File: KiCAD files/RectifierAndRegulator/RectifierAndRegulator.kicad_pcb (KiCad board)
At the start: 2 copper layers, 73.7 x 25.4 mm, 11 parts, among them J1 Input, J2 Output, U1 L7805

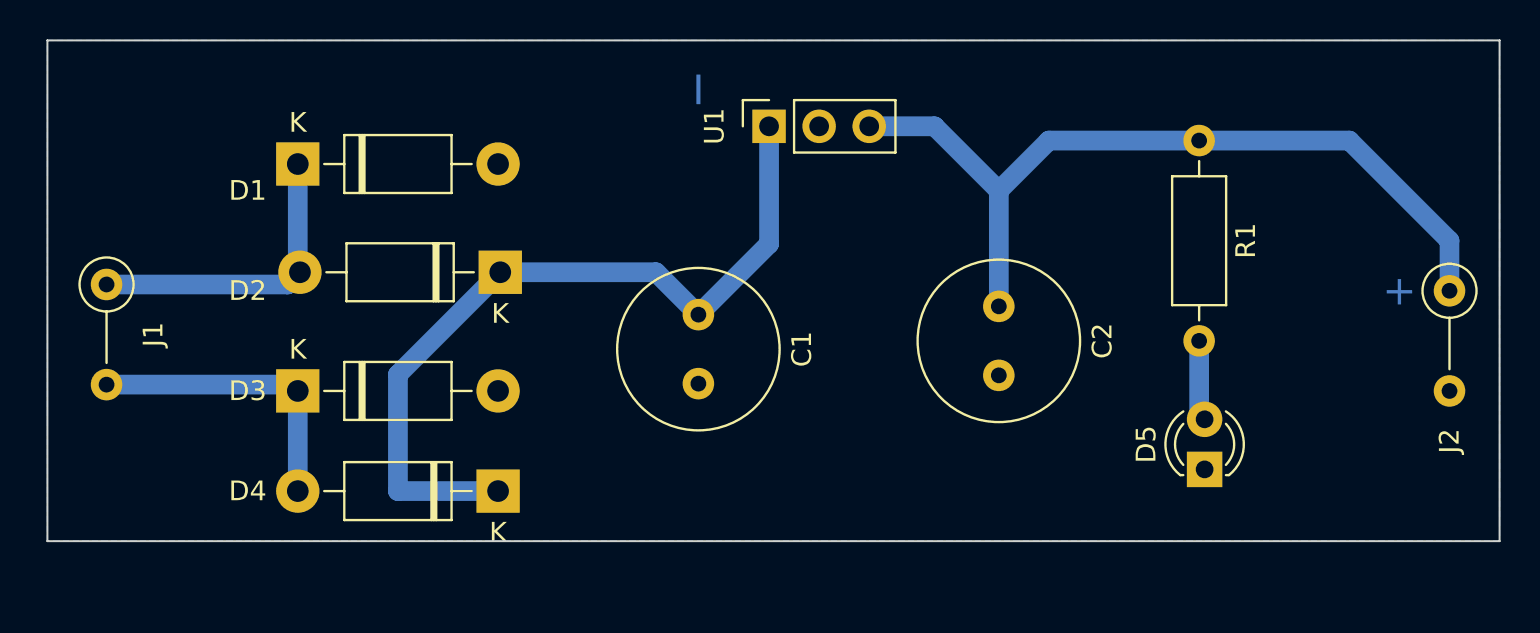
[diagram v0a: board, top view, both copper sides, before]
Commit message: Edited Rectifier schematics and PCB
edited the trackwidth from 1mm to 1.5mm
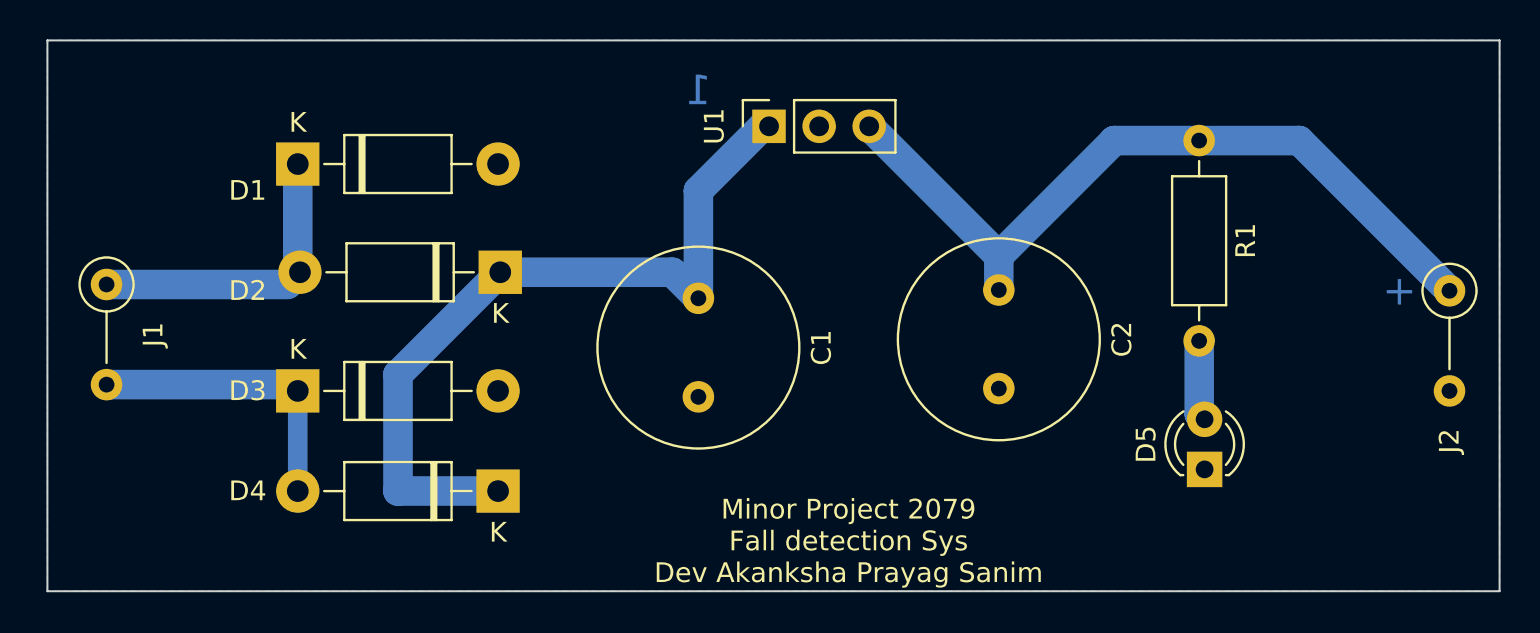
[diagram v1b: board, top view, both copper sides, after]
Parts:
- C1, C2: footprint Capacitor_THT:C_Radial_D8.0mm_H7.0mm_P3.50mm -> Capacitor_THT:C_Radial_D10.0mm_H20.0mm_P5.00mm
- R1: value 470/220 -> 470
- moved C1 0.83 mm to (101.6, 122.3)
- moved C2 0.83 mm to (116.8, 121.9)
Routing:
- net Net-(C2-Pad1): track 42.4 -> 39.5 mm
- net unconnected-(C1-Pad1): track 40.3 -> 39.3 mm
- net GND: track 0.89 -> 0.30 mm
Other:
- board size 73.7 x 25.4 mm -> 73.7 x 27.9 mm
- board text added: "1"
- board text added: "Minor Project 2079 Fall detection Sys Dev Akanksha Prayag Sanim"
- board text removed: "I"

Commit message: Edited PCB
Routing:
- net unconnected-(C1-Pad1): track 39.3 -> 21.1 mm
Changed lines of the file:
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@@
     (effects (font (size 1 1) (thickness 0.15)))
   )
-  (segment (start 81.28 115.49) (end 81.28 120.87) (width 1.5) (layer "B.Cu") (net 1))
+  (segment (start 81.39 120.98) (end 81.39 115.6) (width 1) (layer "B.Cu") (net 1))
+  (segment (start 81.39 115.6) (end 81.28 115.49) (width 1) (layer "B.Cu") (net 1))
   (segment (start 71.58 121.6) (end 80.77 121.6) (width 1.5) (layer "B.Cu") (net 1))
   (segment (start 80.77 121.6) (end 81.39 120.98) (width 1) (layer "B.Cu") (net 1))
   (segment (start 81.28 120.87) (end 81.39 120.98) (width 1.5) (layer "B.Cu") (net 1))
   (segment (start 91.65 126.79) (end 91.44 127) (width 0.25) (layer "B.Cu") (net 2))
-  (segment (start 101.6 116.84) (end 101.6 122.3) (width 1.5) (layer "B.Cu") (net 3))
   (segment (start 105.185 113.5775) (end 104.8625 113.5775) (width 1.5) (layer "B.Cu") (net 3))
-  (segment (start 86.36 126.17) (end 86.36 132.08) (width 1.5) (layer "B.Cu") (net 3))
-  (segment (start 104.8625 113.5775) (end 101.6 116.84) (width 1.5) (layer "B.Cu") (net 3))
-  (segment (start 91.55 120.98) (end 86.36 126.17) (width 1.5) (layer "B.Cu") (net 3))
-  (segment (start 91.55 120.98) (end 100.28 120.98) (width 1.5) (layer "B.Cu") (net 3))
-  (segment (start 86.36 132.08) (end 91.44 132.08) (width 1.5) (layer "B.Cu") (net 3))
-  (segment (start 100.28 120.98) (end 101.6 122.3) (width 1.5) (layer "B.Cu") (net 3))
-  (segment (start 122.6925 114.3) (end 116.84 120.1525) (width 1.5) (layer "B.Cu") (net 4))
-  (segment (start 116.84 121.88) (end 116.84 120.1525) (width 1.5) (layer "B.Cu") (net 4))
-  (segment (start 139.7 121.92) (end 132.08 114.3) (width 1.5) (layer "B.Cu") (net 4))
-  (segment (start 132.08 114.3) (end 127 114.3) (width 1.5) (layer "B.Cu") (net 4))
-  (segment (start 127 114.3) (end 122.6925 114.3) (width 1.5) (layer "B.Cu") (net 4))
-  (segment (start 116.84 120.1525) (end 110.265 113.5775) (width 1.5) (layer "B.Cu") (net 4))
-  (segment (start 127 128.16169) (end 127.277858 128.439548) (width 1.5) (layer "B.Cu") (net 5))
-  (segment (start 127 124.46) (end 127 128.16169) (width 1.5) (layer "B.Cu") (net 5))
+  (segment (start 91.55 120.98) (end 100.28 120.98) (width 1) (layer "B.Cu") (net 3))
+  (segment (start 100.28 120.98) (end 101.6 122.3) (width 1) (layer "B.Cu") (net 3))
+  (segment (start 101.6 122.3) (end 101.6 117.1625) (width 1) (layer "B.Cu") (net 3))
+  (segment (start 101.6 117.1625) (end 105.185 113.5775) (width 1) (layer "B.Cu") (net 3))
+  (segment (start 116.84 120.1525) (end 116.84 121.88) (width 1) (layer "B.Cu") (net 4))
+  (segment (start 122.6925 114.3) (end 116.84 120.1525) (width 1) (layer "B.Cu") (net 4))
+  (segment (start 139.7 121.92) (end 132.08 114.3) (width 1) (layer "B.Cu") (net 4))
+  (segment (start 132.08 114.3) (end 127 114.3) (width 1) (layer "B.Cu") (net 4))
+  (segment (start 127 114.3) (end 122.6925 114.3) (width 1) (layer "B.Cu") (net 4))
+  (segment (start 110.265 113.5775) (end 116.84 120.1525) (width 1) (layer "B.Cu") (net 4))
+  (segment (start 127 128.16169) (end 127.277858 128.439548) (width 1) (layer "B.Cu") (net 5))
+  (segment (start 127 124.46) (end 127 128.16169) (width 1) (layer "B.Cu") (net 5))
   (segment (start 80.96 126.68) (end 81.28 127) (width 1) (layer "B.Cu") (net 6))
   (segment (start 71.58 126.68) (end 80.96 126.68) (width 1.5) (layer "B.Cu") (net 6))
-  (segment (start 81.28 132.08) (end 81.28 127) (width 1) (layer "B.Cu") (net 6))
+  (segment (start 81.28 127) (end 81.28 132.08) (width 1) (layer "B.Cu") (net 6))
   (zone (net 2) (net_name "GND") (layer "B.Cu") (hatch edge 0.508)
     (connect_pads (clearance 0.508))

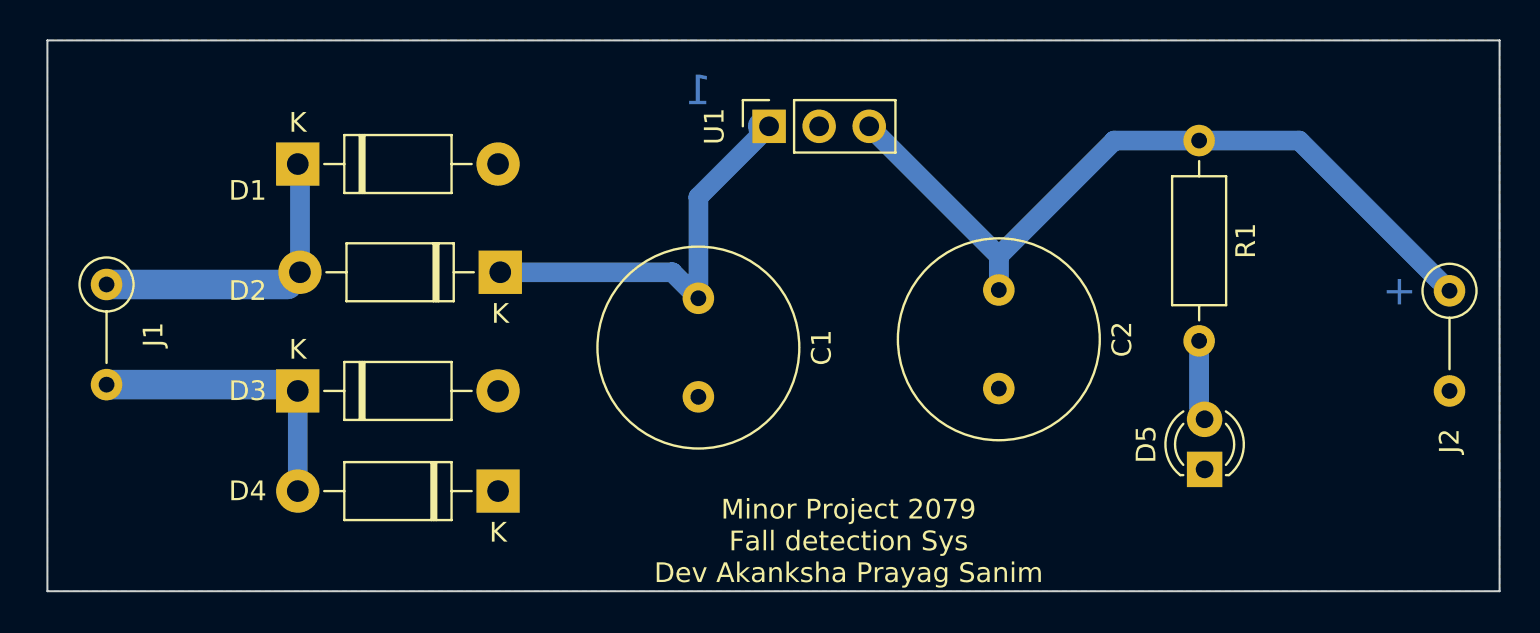
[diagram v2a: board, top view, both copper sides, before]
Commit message: Rectiier ckt bug fixed
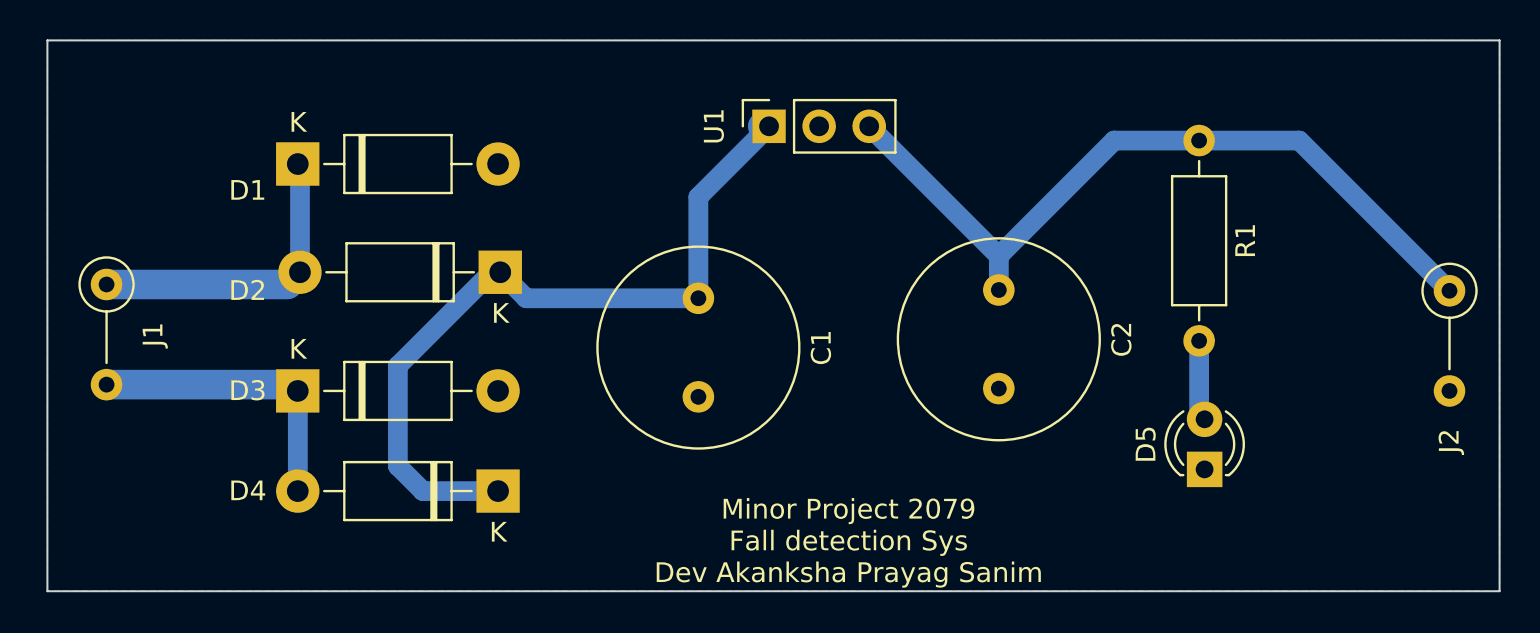
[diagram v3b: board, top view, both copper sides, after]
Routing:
- net unconnected-(C1-Pad1): track 21.1 -> 39.0 mm
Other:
- board text removed: "+"
- board text removed: "1"
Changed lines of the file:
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@@
   )
   (gr_rect (start 68.58 109.22) (end 142.24 137.16) (layer "Edge.Cuts") (width 0.1) (fill none))
-  (gr_text "1\n" (at 101.6 111.76) (layer "B.Cu")
-    (effects (font (size 1.5 1.5) (thickness 0.3)) (justify mirror))
-  )
-  (gr_text "+" (at 137.16 121.92) (layer "B.Cu")
-    (effects (font (size 1.5 1.5) (thickness 0.3)) (justify mirror))
-  )
   (gr_text "Minor Project 2079\nFall detection Sys\nDev Akanksha Prayag Sanim" (at 109.22 134.62) (layer "F.SilkS")
     (effects (font (size 1 1) (thickness 0.15)))
@@
   (segment (start 81.28 120.87) (end 81.39 120.98) (width 1.5) (layer "B.Cu") (net 1))
   (segment (start 91.65 126.79) (end 91.44 127) (width 0.25) (layer "B.Cu") (net 2))
+  (segment (start 91.11 120.98) (end 86.36 125.73) (width 1) (layer "B.Cu") (net 3))
+  (segment (start 92.87 122.3) (end 91.55 120.98) (width 1) (layer "B.Cu") (net 3))
   (segment (start 105.185 113.5775) (end 104.8625 113.5775) (width 1.5) (layer "B.Cu") (net 3))
-  (segment (start 91.55 120.98) (end 100.28 120.98) (width 1) (layer "B.Cu") (net 3))
-  (segment (start 100.28 120.98) (end 101.6 122.3) (width 1) (layer "B.Cu") (net 3))
+  (segment (start 86.36 130.81) (end 87.63 132.08) (width 1) (layer "B.Cu") (net 3))
+  (segment (start 101.6 122.3) (end 92.87 122.3) (width 1) (layer "B.Cu") (net 3))
+  (segment (start 91.55 120.98) (end 91.11 120.98) (width 1) (layer "B.Cu") (net 3))
   (segment (start 101.6 122.3) (end 101.6 117.1625) (width 1) (layer "B.Cu") (net 3))
+  (segment (start 87.63 132.08) (end 91.44 132.08) (width 1) (layer "B.Cu") (net 3))
   (segment (start 101.6 117.1625) (end 105.185 113.5775) (width 1) (layer "B.Cu") (net 3))
+  (segment (start 86.36 125.73) (end 86.36 130.81) (width 1) (layer "B.Cu") (net 3))
   (segment (start 116.84 120.1525) (end 116.84 121.88) (width 1) (layer "B.Cu") (net 4))
   (segment (start 122.6925 114.3) (end 116.84 120.1525) (width 1) (layer "B.Cu") (net 4))

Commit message: Edited rectifier pcb
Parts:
- moved D1 6.59 mm to (81.3, 122.1)
- moved D2 4.14 mm to (91.4, 116.8)
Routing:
- net GND: track 0.30 -> 73.4 mm
- net unconnected-(C1-Pad1): track 39.0 -> 45.4 mm
- net Net-(D1-Pad1): track 15.8 -> 15.1 mm
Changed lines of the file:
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@@
   )
   (footprint "Diode_THT:D_DO-41_SOD81_P10.16mm_Horizontal" (layer "F.Cu")
-    (at 91.55 120.98 180)
+    (at 91.44 116.84 180)
     (descr "Diode, DO-41_SOD81 series, Axial, Horizontal, pin pitch=10.16mm, , length*diameter=5.2*2.7mm^2, , http://www.diodes.com/_files/packages/DO-41%20(Plastic).pdf")
     (tags "Diode DO-41_SOD81 series Axial Horizontal pin pitch 10.16mm  length 5.2mm diameter 2.7mm")
@@
   )
   (footprint "Diode_THT:D_DO-41_SOD81_P10.16mm_Horizontal" (layer "F.Cu")
-    (at 81.28 115.49)
+    (at 81.28 122.08)
     (descr "Diode, DO-41_SOD81 series, Axial, Horizontal, pin pitch=10.16mm, , length*diameter=5.2*2.7mm^2, , http://www.diodes.com/_files/packages/DO-41%20(Plastic).pdf")
     (tags "Diode DO-41_SOD81 series Axial Horizontal pin pitch 10.16mm  length 5.2mm diameter 2.7mm")
@@
     (effects (font (size 1 1) (thickness 0.15)))
   )
-  (segment (start 81.39 120.98) (end 81.39 115.6) (width 1) (layer "B.Cu") (net 1))
-  (segment (start 81.39 115.6) (end 81.28 115.49) (width 1) (layer "B.Cu") (net 1))
-  (segment (start 71.58 121.6) (end 80.77 121.6) (width 1.5) (layer "B.Cu") (net 1))
-  (segment (start 80.77 121.6) (end 81.39 120.98) (width 1) (layer "B.Cu") (net 1))
-  (segment (start 81.28 120.87) (end 81.39 120.98) (width 1.5) (layer "B.Cu") (net 1))
+  (segment (start 80.8 121.6) (end 81.28 122.08) (width 1.5) (layer "B.Cu") (net 1))
+  (segment (start 71.58 121.6) (end 80.8 121.6) (width 1.5) (layer "B.Cu") (net 1))
+  (segment (start 81.28 116.84) (end 81.28 122.08) (width 1) (layer "B.Cu") (net 1))
+  (segment (start 91.74 127.3) (end 91.44 127) (width 1) (layer "B.Cu") (net 2))
+  (segment (start 101.6 127.3) (end 91.74 127.3) (width 1) (layer "B.Cu") (net 2))
+  (segment (start 127.277858 130.979548) (end 135.720452 130.979548) (width 1) (layer "B.Cu") (net 2))
+  (segment (start 107.725 121.175) (end 101.6 127.3) (width 1) (layer "B.Cu") (net 2))
+  (segment (start 116.42 127.3) (end 116.84 126.88) (width 1) (layer "B.Cu") (net 2))
   (segment (start 91.65 126.79) (end 91.44 127) (width 0.25) (layer "B.Cu") (net 2))
-  (segment (start 91.11 120.98) (end 86.36 125.73) (width 1) (layer "B.Cu") (net 3))
-  (segment (start 92.87 122.3) (end 91.55 120.98) (width 1) (layer "B.Cu") (net 3))
+  (segment (start 135.720452 130.979548) (end 139.7 127) (width 1) (layer "B.Cu") (net 2))
+  (segment (start 101.6 127.3) (end 116.42 127.3) (width 1) (layer "B.Cu") (net 2))
+  (segment (start 120.939548 130.979548) (end 116.84 126.88) (width 1) (layer "B.Cu") (net 2))
+  (segment (start 91.44 122.08) (end 91.44 127) (width 1) (layer "B.Cu") (net 2))
+  (segment (start 127.277858 130.979548) (end 120.939548 130.979548) (width 1) (layer "B.Cu") (net 2))
+  (segment (start 107.725 113.5775) (end 107.725 121.175) (width 1) (layer "B.Cu") (net 2))
+  (segment (start 96.14 116.84) (end 101.6 122.3) (width 1) (layer "B.Cu") (net 3))
   (segment (start 105.185 113.5775) (end 104.8625 113.5775) (width 1.5) (layer "B.Cu") (net 3))
-  (segment (start 86.36 130.81) (end 87.63 132.08) (width 1) (layer "B.Cu") (net 3))
-  (segment (start 101.6 122.3) (end 92.87 122.3) (width 1) (layer "B.Cu") (net 3))
-  (segment (start 91.55 120.98) (end 91.11 120.98) (width 1) (layer "B.Cu") (net 3))
+  (segment (start 88.9 116.84) (end 91.44 116.84) (width 1) (layer "B.Cu") (net 3))
+  (segment (start 91.44 132.08) (end 88.9 132.08) (width 1) (layer "B.Cu") (net 3))
+  (segment (start 86.36 129.54) (end 86.36 119.38) (width 1) (layer "B.Cu") (net 3))
+  (segment (start 86.36 119.38) (end 88.9 116.84) (width 1) (layer "B.Cu") (net 3))
+  (segment (start 88.9 132.08) (end 86.36 129.54) (width 1) (layer "B.Cu") (net 3))
+  (segment (start 91.44 116.84) (end 96.14 116.84) (width 1) (layer "B.Cu") (net 3))
   (segment (start 101.6 122.3) (end 101.6 117.1625) (width 1) (layer "B.Cu") (net 3))
-  (segment (start 87.63 132.08) (end 91.44 132.08) (width 1) (layer "B.Cu") (net 3))
   (segment (start 101.6 117.1625) (end 105.185 113.5775) (width 1) (layer "B.Cu") (net 3))
-  (segment (start 86.36 125.73) (end 86.36 130.81) (width 1) (layer "B.Cu") (net 3))
   (segment (start 116.84 120.1525) (end 116.84 121.88) (width 1) (layer "B.Cu") (net 4))
   (segment (start 122.6925 114.3) (end 116.84 120.1525) (width 1) (layer "B.Cu") (net 4))
@@
     (connect_pads (clearance 0.508))
     (min_thickness 0.254) (filled_areas_thickness no)
-    (fill yes (thermal_gap 0.508) (thermal_bridge_width 0.508))
+    (fill (thermal_gap 0.508) (thermal_bridge_width 0.508))
     (polygon
       (pts

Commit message: halka edit smoothing capacitor ma
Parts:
- added C3: , Capacitor_THT:CP_Radial_D5.0mm_P2.50mm, F.Cu at (119.4, 120.0)
- C1: value 1000uF -> (none); footprint Capacitor_THT:C_Radial_D10.0mm_H20.0mm_P5.00mm -> Capacitor_THT:CP_Radial_D8.0mm_P2.50mm
- C2: value 1000uF -> (none); footprint Capacitor_THT:C_Radial_D10.0mm_H20.0mm_P5.00mm -> Capacitor_THT:CP_Radial_D6.3mm_P2.50mm
- moved C2 10.2 mm to (106.6, 121.9), turned to 0 degrees
- moved C1 2.68 mm to (99.1, 123.2)
- moved U1 2.54 mm to (107.7, 113.6)
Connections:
- C1 pad 1: unconnected-(C1-Pad1) -> Net-(C1-Pad1)
- C2 pad 1: Net-(C2-Pad1) -> Net-(C1-Pad1)
- D2 pad 1: unconnected-(C1-Pad1) -> Net-(C1-Pad1)
- D4 pad 1: unconnected-(C1-Pad1) -> Net-(C1-Pad1)
- J2 pad 1: Net-(C2-Pad1) -> Net-(C3-Pad1)
- R1 pad 1: Net-(C2-Pad1) -> Net-(C3-Pad1)
- U1 pad 1: unconnected-(C1-Pad1) -> Net-(C1-Pad1)
- U1 pad 3: Net-(C2-Pad1) -> Net-(C3-Pad1)
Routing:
- net Net-(C1-Pad1): track 0.00 -> 50.3 mm
- net unconnected-(C1-Pad1): track 45.4 -> 0.00 mm
- net Net-(C2-Pad1): track 39.5 -> 0.00 mm
- net Net-(C3-Pad1): track 0.00 -> 37.0 mm
- net GND: track 73.4 -> 77.9 mm
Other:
- board text added: "Minor Project 2079 Fall detection Sys Akanksha Devraj Prayag Sanim"
- board text removed: "Minor Project 2079 Fall detection Sys Dev Akanksha Prayag Sanim"
